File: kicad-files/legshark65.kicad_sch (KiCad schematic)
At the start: 157 parts, among them SW1 K2-1187SQ-A4SW-06, SW2 PCM12SMTR, T2 53261-0471, U1 STM32F411CEU6, U3 AT24C256C-SSHL-T, Y1 TAXM8M4RFDCET2T

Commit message: Update schematic to noLED MX only footpints
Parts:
- K_0, K_1, K_10, K_11, K_12, K_13, K_14, K_16, K_17, K_18, K_19, K_2, K_20, K_21, K_22, K_23, K_24, K_25, K_26, K_27, K_28, K_29, K_3, K_30, K_31, K_32, K_33, K_34, K_35, K_36, K_37, K_38, K_39, K_4, K_40, K_41, K_44, K_45, K_46, K_47, K_48, K_49, K_5, K_50, K_51, K_52, K_53, K_54, K_55, K_56, K_6, K_64, K_7, K_8, K_9: footprint MX_Alps_Hybrid:MX-1U-NoLED -> MX_Only:MXOnly-1U-NoLED
- K_15, K_42, K_43: footprint MX_Alps_Hybrid:MX-2U-NoLED -> MX_Only:MXOnly-2U-NoLED
- K_57: footprint MX_Alps_Hybrid:MX-1.75U-NoLED -> MX_Only:MXOnly-1.75U-NoLED
- K_58, K_59, K_62, K_63: footprint MX_Alps_Hybrid:MX-1.25U-NoLED -> MX_Only:MXOnly-1.25U-NoLED
- K_60: footprint MX_Alps_Hybrid:MX-2.25U-NoLED -> MX_Only:MXOnly-2.25U-ReversedStabilizers-NoLED
- K_61: footprint MX_Alps_Hybrid:MX-3U-NoLED -> MX_Only:MXOnly-3U-ReversedStabilizers-NoLED
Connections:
- net col0 renamed c0
- net col1 renamed c1
- net col10 renamed c10
- net col11 renamed c11
- net col12 renamed c12
- net col13 renamed c13
- net col14 renamed c14
- net col2 renamed c2
- net col3 renamed c3
- net col4 renamed c4
- net col5 renamed c5
- net col6 renamed c6
- net col7 renamed c7
- net col8 renamed c8
- net col9 renamed c9
- net row0 renamed r0
- net row1 renamed r1
- net row2 renamed r2
- net row3 renamed r3
- net row4 renamed r4

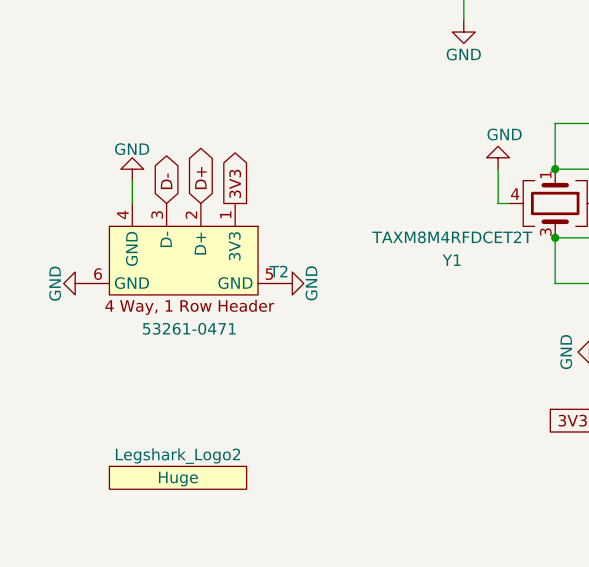
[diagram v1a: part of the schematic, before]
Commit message: Updated PCB design constraints
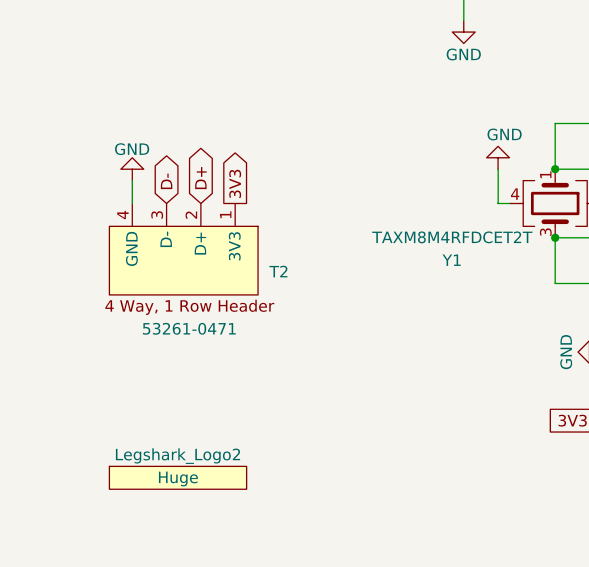
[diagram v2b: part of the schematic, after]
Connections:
- net GND: no longer T2.5 (GND), T2.6 (GND)
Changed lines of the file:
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@@
-    )
-  )
-  (symbol (lib_id "power:GND") (at 41.91 264.16 270) (unit 1)
-    (in_bom yes) (on_board yes) (dnp no)
-    (property "Reference" "#PWR037" (at 35.56 264.16 0)
-      (effects (font (size 1.27 1.27)) hide)
-    )
-    (property "Value" "GND" (at 38.4603 266.1746 0)
-      (effects (font (size 1.27 1.27)) (justify right))
-    )
-    (property "Footprint" "" (at 41.91 264.16 0)
-      (effects (font (size 1.27 1.27)) hide)
-    )
-    (property "Datasheet" "" (at 41.91 264.16 0)
-      (effects (font (size 1.27 1.27)) hide)
-    )
-    (pin "1")
-    (instances
-      (project "old_layout"
-        (path "/2fda2561-53ed-4930-8b41-858e0e3dd5f4"
-          (reference "#PWR037") (unit 1)
-        )
-      )
-      (project "legshark65"
-        (path "/9ddf6dc5-8b5e-413a-9b25-d1d5a5a60469"
-          (reference "#PWR01") (unit 1)
-        )
-      )
     )
   )
@@
       (effects (font (size 1.27 1.27)) hide)
     )
-    (pin "5")
-    (pin "6")
     (pin "1")
     (pin "2")
@@
         )
       )
-    )
-  )
-  (symbol (lib_id "power:GND") (at 63.5 264.16 90) (unit 1)
-    (in_bom yes) (on_board yes) (dnp no)
-    (property "Reference" "#PWR036" (at 69.85 264.16 0)
-      (effects (font (size 1.27 1.27)) hide)
-    )
-    (property "Value" "GND" (at 66.9497 262.1454 0)
-      (effects (font (size 1.27 1.27)) (justify right))
-    )
-    (property "Footprint" "" (at 63.5 264.16 0)
-      (effects (font (size 1.27 1.27)) hide)
-    )
-    (property "Datasheet" "" (at 63.5 264.16 0)
-      (effects (font (size 1.27 1.27)) hide)
-    )
-    (pin "1")
-    (instances
-      (project "old_layout"
-        (path "/2fda2561-53ed-4930-8b41-858e0e3dd5f4"
-          (reference "#PWR036") (unit 1)
-        )
-      )
-      (project "legshark65"
-        (path "/9ddf6dc5-8b5e-413a-9b25-d1d5a5a60469"
-          (reference "#PWR03") (unit 1)
-        )
-      )

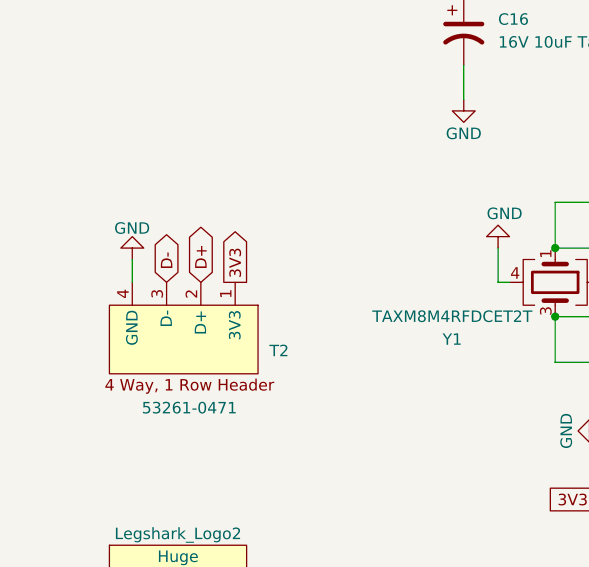
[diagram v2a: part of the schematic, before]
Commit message: Connected most of the rows and cols
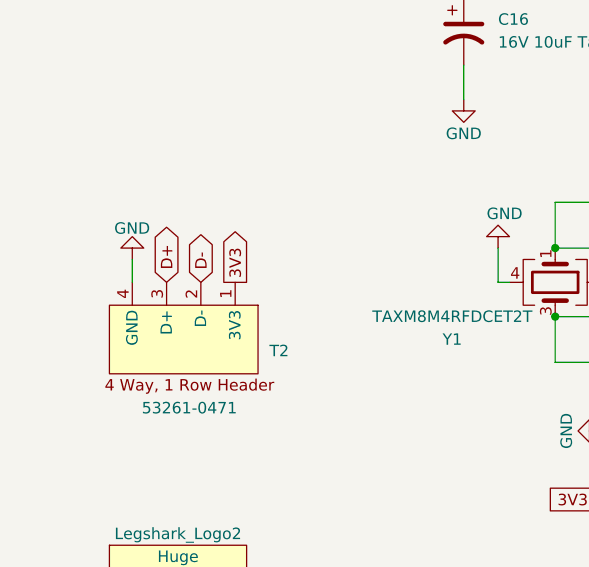
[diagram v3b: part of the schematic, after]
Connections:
- net D+: now also T2.3 (D+); no longer T2.2 (D+)
- net D-: now also T2.2 (D-); no longer T2.3 (D-)
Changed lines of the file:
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@@
     )
   )
-  (global_label "D-" (shape bidirectional) (at 50.8 255.27 90) (fields_autoplaced)
+  (global_label "D-" (shape bidirectional) (at 54.61 255.27 90) (fields_autoplaced)
+    (effects (font (size 1.27 1.27)) (justify left))
+    (property "Intersheetrefs" "${INTERSHEET_REFS}" (at 54.61 249.2235 90)
+      (effects (font (size 1.27 1.27)) (justify left) hide)
+    )
+  )
+  (global_label "D+" (shape bidirectional) (at 50.8 255.27 90) (fields_autoplaced)
     (effects (font (size 1.27 1.27)) (justify left))
     (property "Intersheetrefs" "${INTERSHEET_REFS}" (at 50.8 249.2235 90)
       (effects (font (size 1.27 1.27)) (justify left) hide)
     )
-  )
-  (global_label "D+" (shape bidirectional) (at 54.61 255.27 90) (fields_autoplaced)
-    (effects (font (size 1.27 1.27)) (justify left))
-    (property "Intersheetrefs" "${INTERSHEET_REFS}" (at 54.61 249.2235 90)
-      (effects (font (size 1.27 1.27)) (justify left) hide)
-    )

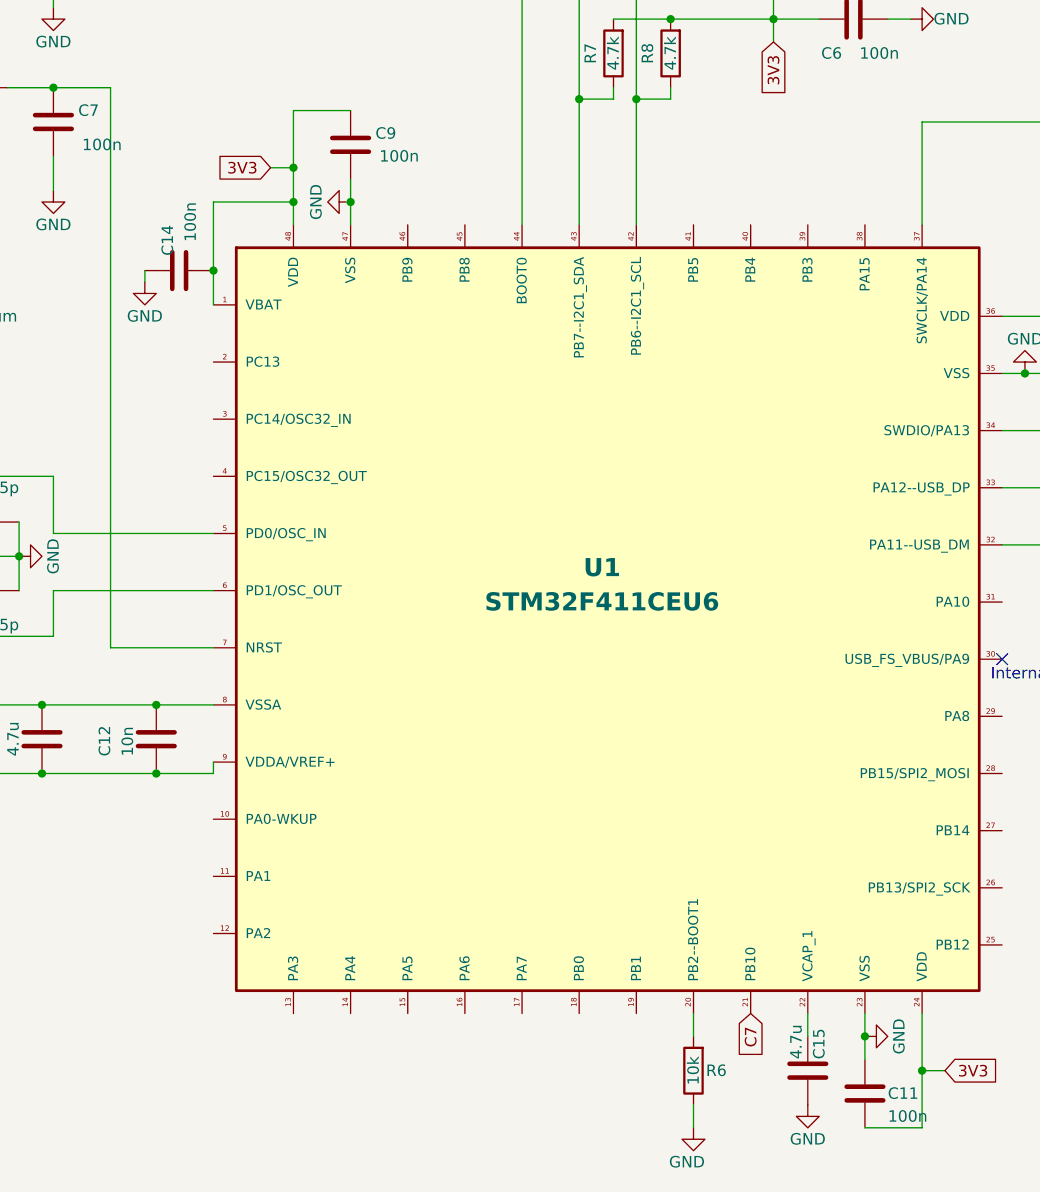
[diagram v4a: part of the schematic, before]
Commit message: Started connecting cols
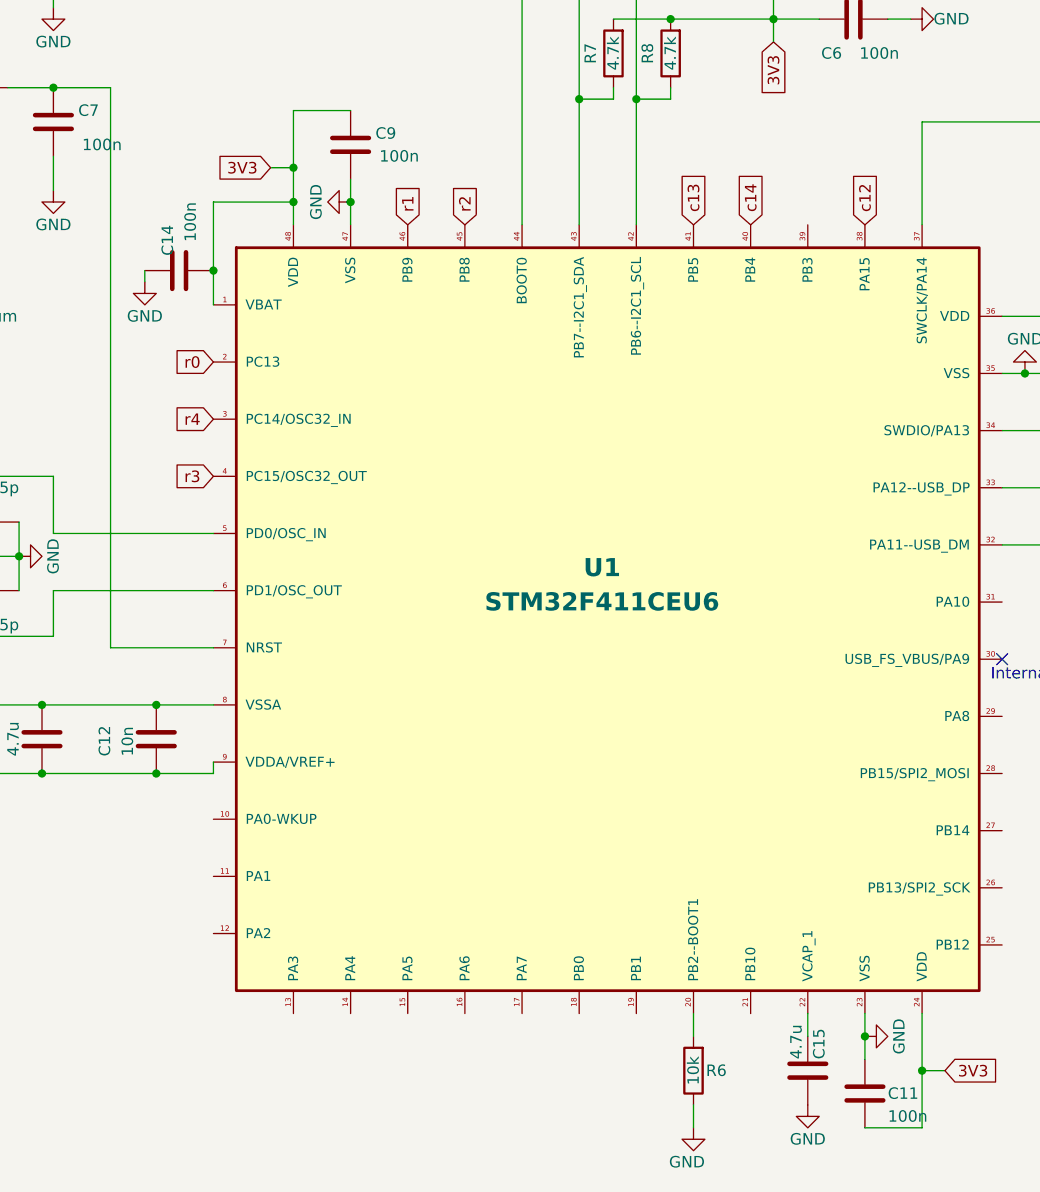
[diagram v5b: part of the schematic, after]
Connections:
- net c12: now also U1.38 (PA15)
- net c13: now also U1.41 (PB5)
- net c14: now also U1.40 (PB4)
- net r0: now also U1.2 (PC13)
- net r1: now also U1.46 (PB9)
- net r2: now also U1.45 (PB8)
- net r3: now also U1.4 (PC15/OSC32_OUT)
- net r4: now also U1.3 (PC14/OSC32_IN)
- net C7: no longer names the net of U1.21 (PB10)
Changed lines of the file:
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@@
+    )
+  )
+  (global_label "c12" (shape input) (at 199.39 218.44 90) (fields_autoplaced)
+    (effects (font (size 1.27 1.27)) (justify left))
+    (property "Intersheetrefs" "${INTERSHEET_REFS}" (at 199.39 212.6808 90)
+      (effects (font (size 1.27 1.27)) (justify left) hide)
+    )
+  )
+  (global_label "r0" (shape input) (at 127 233.68 180) (fields_autoplaced)
+    (effects (font (size 1.27 1.27)) (justify right))
+    (property "Intersheetrefs" "${INTERSHEET_REFS}" (at 122.7527 233.68 0)
+      (effects (font (size 1.27 1.27)) (justify right) hide)
     )
   )
@@
     )
   )
+  (global_label "r1" (shape input) (at 148.59 218.44 90) (fields_autoplaced)
+    (effects (font (size 1.27 1.27)) (justify left))
+    (property "Intersheetrefs" "${INTERSHEET_REFS}" (at 148.59 214.1927 90)
+      (effects (font (size 1.27 1.27)) (justify left) hide)
+    )
+  )
+  (global_label "r3" (shape input) (at 127 246.38 180) (fields_autoplaced)
+    (effects (font (size 1.27 1.27)) (justify right))
+    (property "Intersheetrefs" "${INTERSHEET_REFS}" (at 122.7527 246.38 0)
+      (effects (font (size 1.27 1.27)) (justify right) hide)
+    )
+  )
   (global_label "3V3" (shape input) (at 78.74 184.15 180) (fields_autoplaced)
     (effects (font (size 1.27 1.27)) (justify right))
@@
     )
   )
+  (global_label "c14" (shape input) (at 186.69 218.44 90) (fields_autoplaced)
+    (effects (font (size 1.27 1.27)) (justify left))
+    (property "Intersheetrefs" "${INTERSHEET_REFS}" (at 186.69 212.6808 90)
+      (effects (font (size 1.27 1.27)) (justify left) hide)
+    )
+  )
   (global_label "c3" (shape input) (at 139.065 27.305 180)
     (effects (font (size 1.27 1.27)) (justify right))
@@
     )
   )
-  (global_label "C7" (shape input) (at 186.69 306.07 270) (fields_autoplaced)
+  (global_label "r4" (shape input) (at 127 240.03 180) (fields_autoplaced)
     (effects (font (size 1.27 1.27)) (justify right))
-    (property "Intersheetrefs" "${INTERSHEET_REFS}" (at 186.69 310.8011 90)
+    (property "Intersheetrefs" "${INTERSHEET_REFS}" (at 122.7527 240.03 0)
       (effects (font (size 1.27 1.27)) (justify right) hide)
+    )
+  )
+  (global_label "c13" (shape input) (at 180.34 218.44 90) (fields_autoplaced)
+    (effects (font (size 1.27 1.27)) (justify left))
+    (property "Intersheetrefs" "${INTERSHEET_REFS}" (at 180.34 212.6808 90)
+      (effects (font (size 1.27 1.27)) (justify left) hide)
     )
   )
@@
       (effects (font (size 1.27 1.27)) (justify left) hide)
     )
+  )
+  (global_label "r2" (shape input) (at 154.94 218.44 90) (fields_autoplaced)
+    (effects (font (size 1.27 1.27)) (justify left))
+    (property "Intersheetrefs" "${INTERSHEET_REFS}" (at 154.94 214.1927 90)
+      (effects (font (size 1.27 1.27)) (justify left) hide)
+    )
